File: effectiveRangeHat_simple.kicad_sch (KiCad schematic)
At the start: 11 parts, among them J1 Raspberry_Pi_2_3, P1 USB4105GFA120

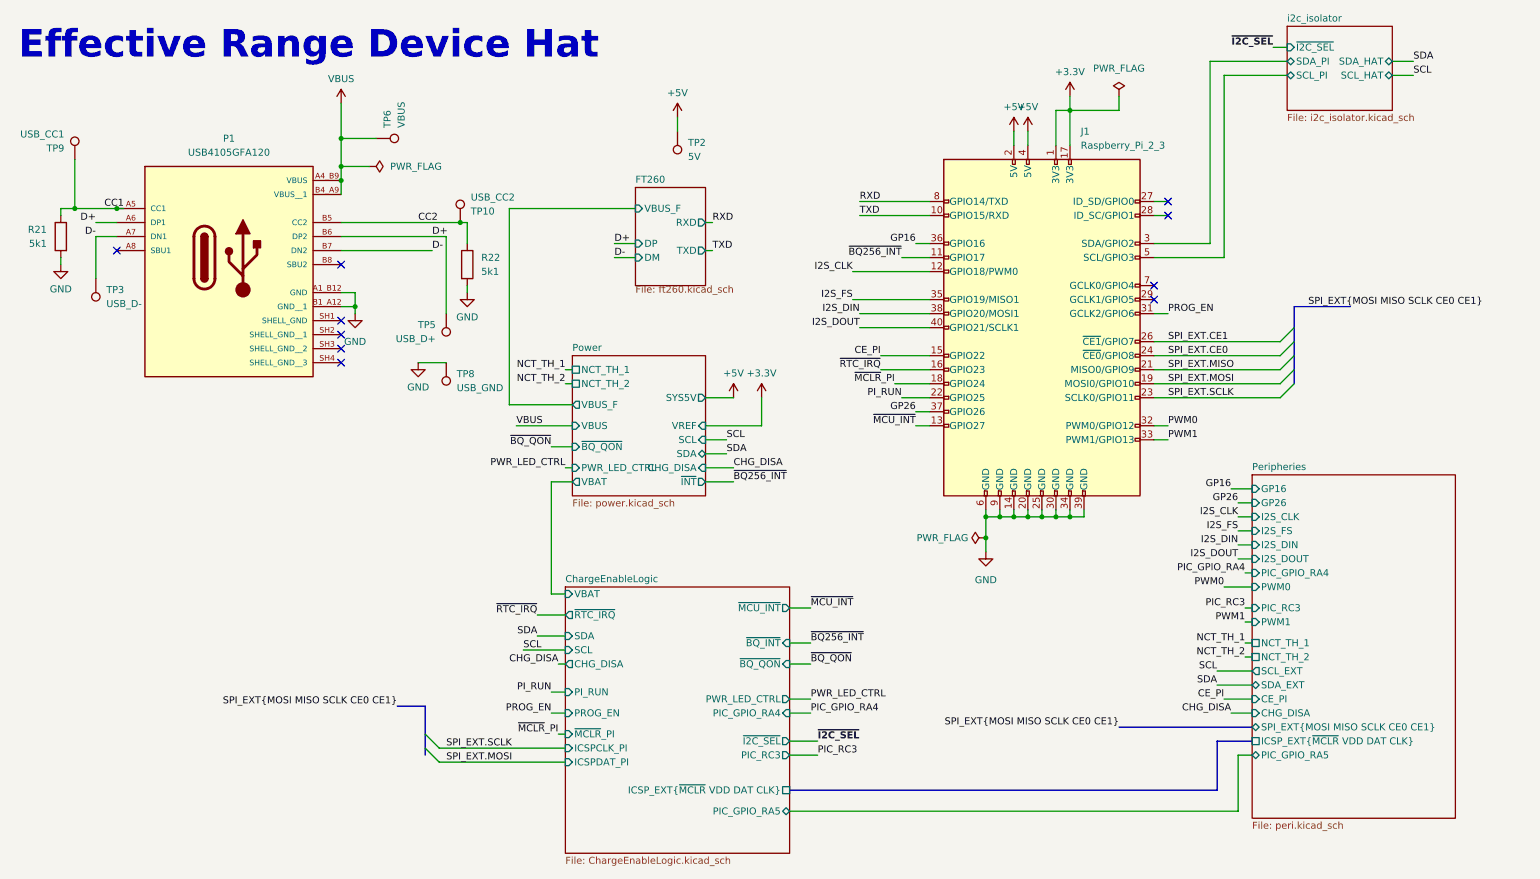
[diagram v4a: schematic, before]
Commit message: feat: 3V3 regulator + complete rework to 16 layers
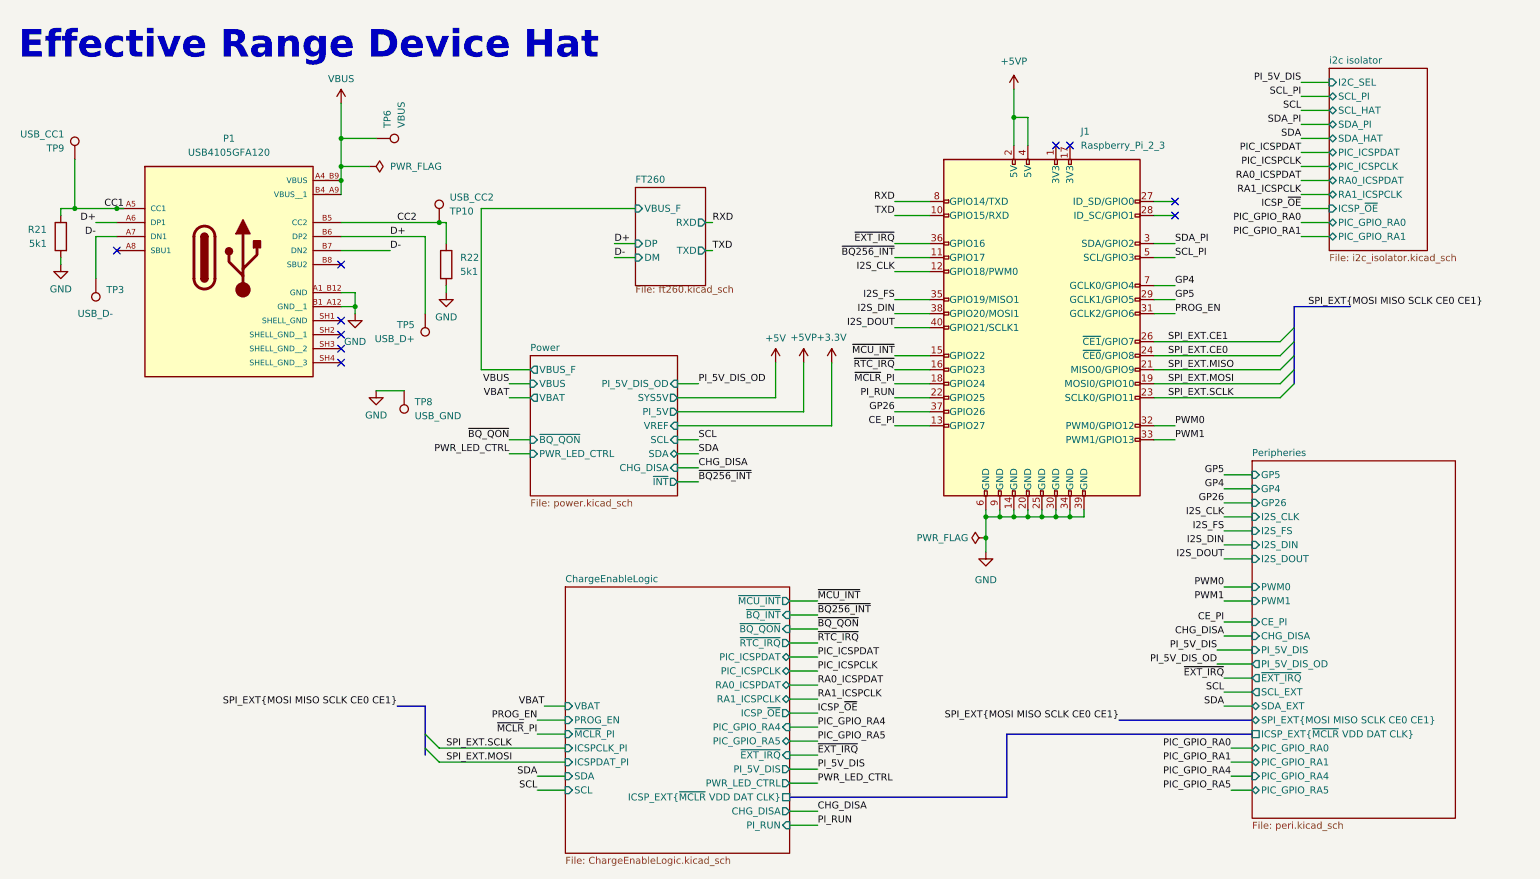
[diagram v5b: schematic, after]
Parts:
- removed TP2: 5V, TestPoint:TestPoint_Pad_D1.0mm, symbol Connector:TestPoint
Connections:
- net +3.3V: no longer J1.1 (3V3), J1.17 (3V3)
- net +5V: no longer J1.2 (5V), J1.4 (5V)
- net CE_PI: now also J1.13 (GPIO27); no longer J1.15 (GPIO22)
- net ~{MCU_INT}: now also J1.15 (GPIO22); no longer J1.13 (GPIO27)
- net GP5: now reaches J1.29 (GCLK1/GPIO5)
- net GP4: now reaches J1.7 (GCLK0/GPIO4)
- net GP16 renamed ~{EXT_IRQ}
- net i2c_isolator/SCL_PI renamed SCL_PI
- net i2c_isolator/SDA_PI renamed SDA_PI
- new net +5VP: J1.2 (5V), J1.4 (5V)
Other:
- removed sheet i2c_isolator
- added sheet i2c isolator (i2c_isolator.kicad_sch)
- sheet ChargeEnableLogic ports: added ICSP_~{OE}, PIC_ICSPCLK, PIC_ICSPDAT, PI_5V_DIS, RA0_ICSPDAT, RA1_ICSPCLK, ~{EXT_IRQ}; removed PIC_RC3, ~{I2C_SEL}
- sheet Peripheries ports: added GP4, GP5, PIC_GPIO_RA0, PIC_GPIO_RA1, PI_5V_DIS, PI_5V_DIS_OD, ~{EXT_IRQ}; removed GP16, NCT_TH_1, NCT_TH_2, PIC_RC3
- sheet Power ports: added PI_5V, PI_5V_DIS_OD; removed NCT_TH_1, NCT_TH_2
- moved on the sheet: R22, TP10, TP5, TP8
